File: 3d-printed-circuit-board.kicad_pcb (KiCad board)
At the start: 2 copper layers, 73.8 x 59.5 mm, 18 parts

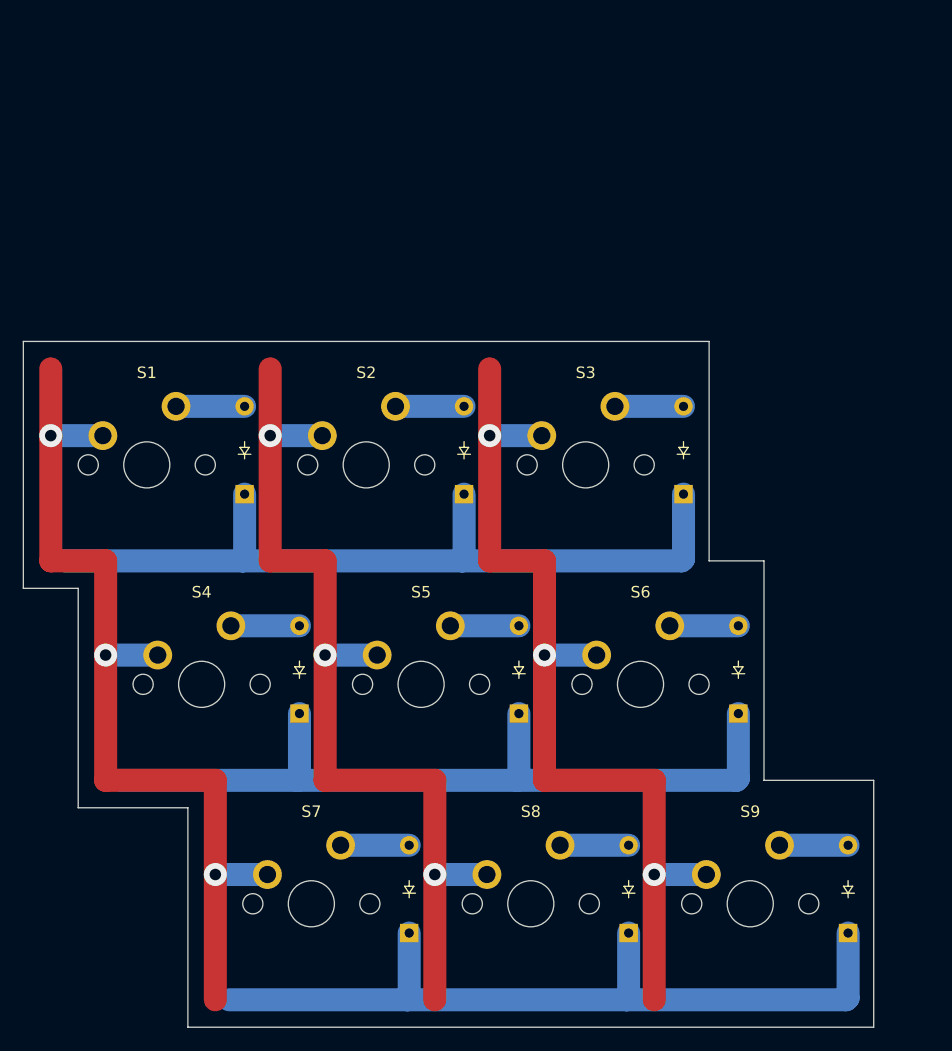
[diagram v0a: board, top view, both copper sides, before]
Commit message: Add MCU footprint
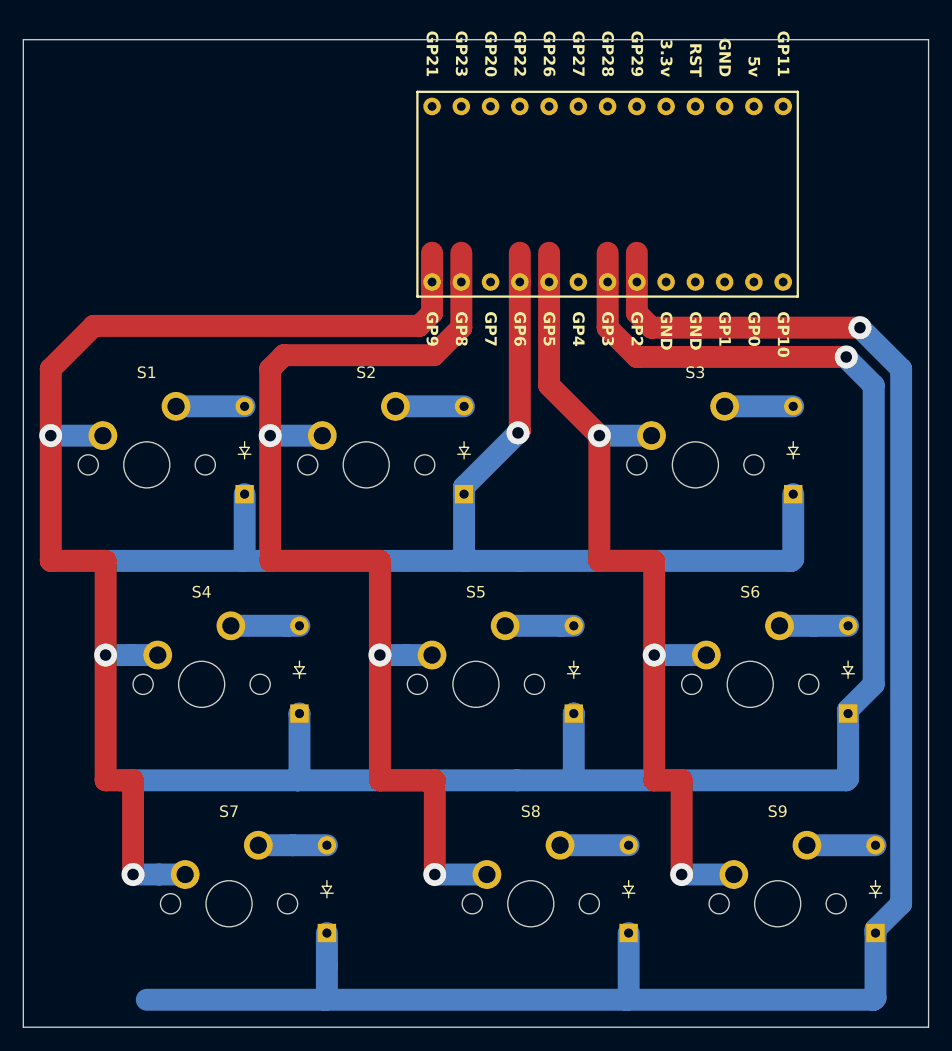
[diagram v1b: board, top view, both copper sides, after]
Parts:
- added U1: Arduino_Pro_Micro, ScottoKeebs_MCU:RP2040_Pro_Micro_Custom, B.Cu at (152.1, 66.9)
- moved S3 9.53 mm to (161.0, 90.4)
- moved S6 9.53 mm to (165.7, 109.4)
- moved D3 9.53 mm to (169.5, 92.9)
- moved D6 9.53 mm to (174.2, 112.0)
- moved D7 7.14 mm to (129.0, 131.0)
- moved S7 7.14 mm to (120.5, 128.5)
- moved S5 4.76 mm to (141.9, 109.4)
- moved D5 4.76 mm to (150.4, 112.0)
- moved S9 2.38 mm to (168.1, 128.5)
- moved D9 2.38 mm to (176.6, 131.0)
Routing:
- net ROW2: track 71.2 -> 163.4 mm, vias 0 -> 1
- net ROW1: track 71.2 -> 141.5 mm, vias 0 -> 1
- net ROW0: track 71.2 -> 103.6 mm, vias 0 -> 1
- net COL0: track 82.9 -> 109.5 mm
- net COL1: track 82.9 -> 98.7 mm
- net COL2: track 82.6 -> 76.3 mm
- net Net-(D6-A): track 5.95 -> 8.93 mm
- net Net-(D7-A): track 5.95 -> 8.93 mm
- net Net-(D5-A): track 5.95 -> 7.06 mm
- net Net-(D4-A): track 5.95 -> 7.06 mm
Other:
- board size 73.8 x 59.5 mm -> 78.6 x 85.7 mm

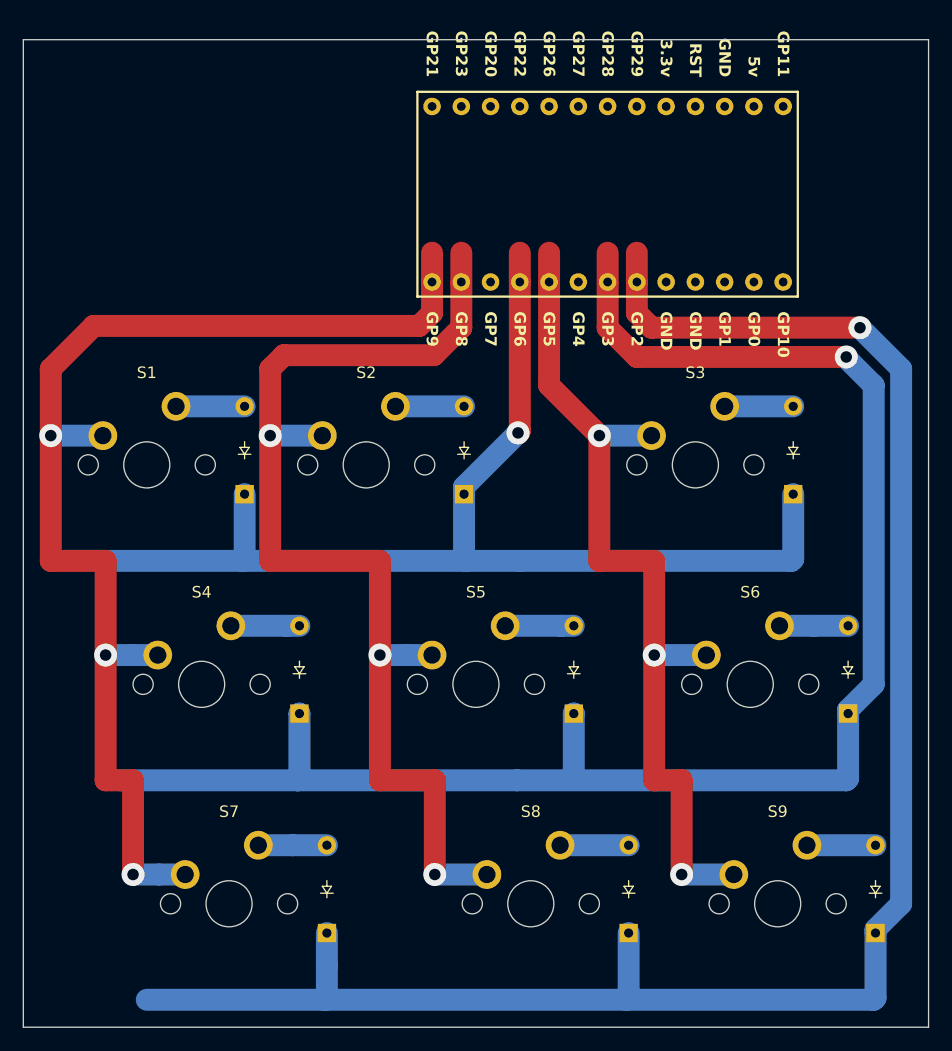
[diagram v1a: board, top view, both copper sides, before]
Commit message: Revise routing to reduce solder points
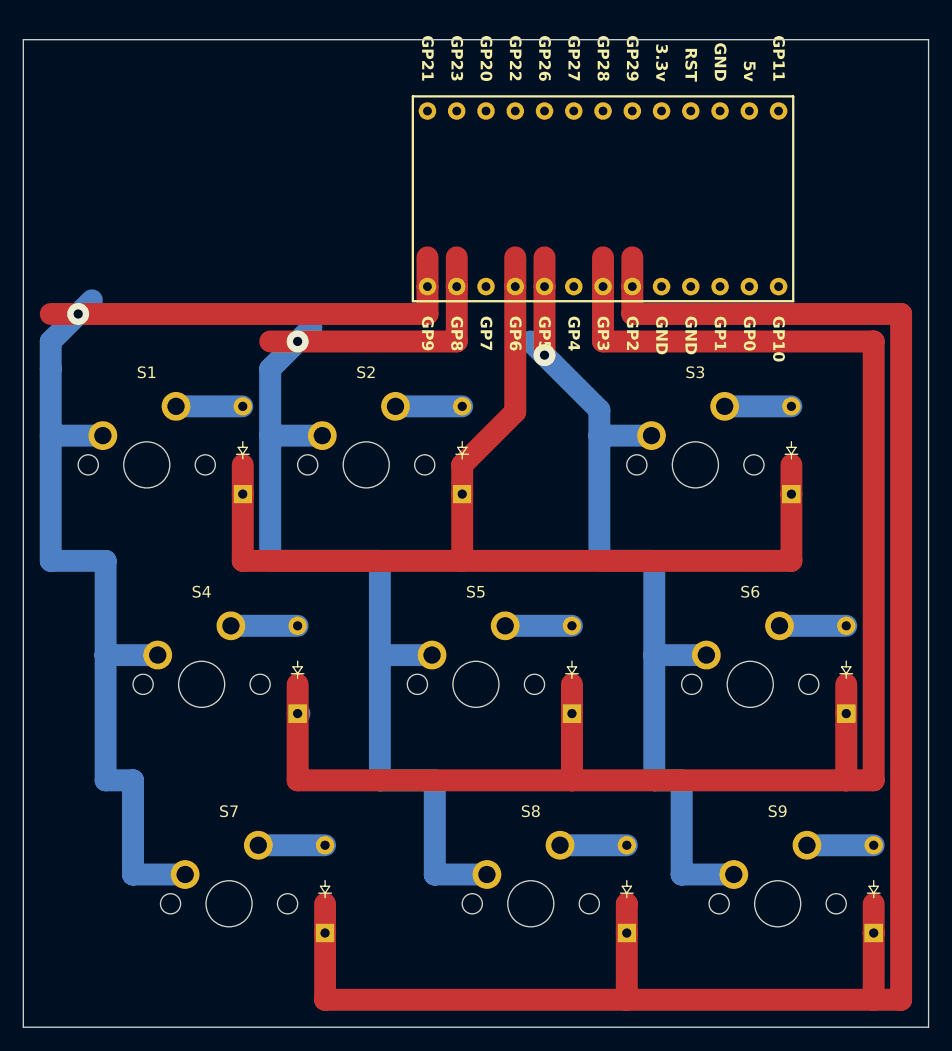
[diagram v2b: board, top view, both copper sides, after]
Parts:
- moved U1 0.56 mm to (151.7, 67.3)
- moved D1 0.16 mm to (121.7, 92.9)
- moved D2 0.16 mm to (140.7, 92.9)
- moved D3 0.16 mm to (169.3, 92.9)
- moved D4 0.16 mm to (126.4, 112.0)
- moved D5 0.16 mm to (150.3, 112.0)
- moved D6 0.16 mm to (174.1, 112.0)
- moved D7 0.16 mm to (128.8, 131.0)
- moved D8 0.16 mm to (155.0, 131.0)
- moved D9 0.16 mm to (176.4, 131.0)
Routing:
- net ROW0: track 103.6 -> 92.6 mm, vias 1 -> 0
- net Net-(D6-A): track 8.93 -> 5.79 mm
- net Net-(D7-A): track 8.93 -> 5.79 mm
- net ROW1: track 141.5 -> 143.9 mm, vias 1 -> 0
- net COL1: track 98.7 -> 100.3 mm, vias 3 -> 1
- net COL2: track 76.3 -> 78.0 mm, vias 3 -> 1
- net Net-(D5-A): track 7.06 -> 5.79 mm
- net Net-(D4-A): track 7.06 -> 5.79 mm
- net ROW2: track 163.4 -> 162.8 mm, vias 1 -> 0
- net COL0: track 109.5 -> 109.7 mm, vias 3 -> 1

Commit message: Route full hhkb layout
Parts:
- added D10: Diode, ScottoKeebs_Components:Diode_DO-35, B.Cu at (217.8, 40.6)
- added D11: Diode, ScottoKeebs_Components:Diode_DO-35, B.Cu at (236.9, 40.6)
- added D12: Diode, ScottoKeebs_Components:Diode_DO-35, B.Cu at (255.9, 40.6)
- added D13: Diode, ScottoKeebs_Components:Diode_DO-35, B.Cu at (275.0, 40.6)
- added D14: Diode, ScottoKeebs_Components:Diode_DO-35, B.Cu at (293.7, 24.1)
- added D16: Diode, ScottoKeebs_Components:Diode_DO-35, B.Cu at (51.1, 59.7)
- added D17: Diode, ScottoKeebs_Components:Diode_DO-35, B.Cu at (74.9, 59.7)
- added D18: Diode, ScottoKeebs_Components:Diode_DO-35, B.Cu at (94.0, 59.7)
- added D19: Diode, ScottoKeebs_Components:Diode_DO-35, B.Cu at (113.0, 59.7)
- added D20: Diode, ScottoKeebs_Components:Diode_DO-35, B.Cu at (132.1, 59.7)
- added D21: Diode, ScottoKeebs_Components:Diode_DO-35, B.Cu at (151.1, 59.7)
- added D22: Diode, ScottoKeebs_Components:Diode_DO-35, B.Cu at (170.2, 59.7)
- added D23: Diode, ScottoKeebs_Components:Diode_DO-35, B.Cu at (189.2, 59.7)
- added D24: Diode, ScottoKeebs_Components:Diode_DO-35, B.Cu at (208.3, 59.7)
- added D25: Diode, ScottoKeebs_Components:Diode_DO-35, B.Cu at (227.3, 59.7)
- added D26: Diode, ScottoKeebs_Components:Diode_DO-35, B.Cu at (246.4, 59.7)
- added D27: Diode, ScottoKeebs_Components:Diode_DO-35, B.Cu at (265.4, 59.7)
- added D28: Diode, ScottoKeebs_Components:Diode_DO-35, B.Cu at (284.5, 59.7)
- added D29: Diode, ScottoKeebs_Components:Diode_DO-35, B.Cu at (308.3, 59.7)
- added D30: Diode, ScottoKeebs_Components:Diode_DO-35, B.Cu at (53.5, 78.7)
- added D31: Diode, ScottoKeebs_Components:Diode_DO-35, B.Cu at (79.7, 78.7)
- added D32: Diode, ScottoKeebs_Components:Diode_DO-35, B.Cu at (98.7, 78.7)
- added D33: Diode, ScottoKeebs_Components:Diode_DO-35, B.Cu at (117.8, 78.7)
- added D34: Diode, ScottoKeebs_Components:Diode_DO-35, B.Cu at (136.8, 78.7)
- added D35: Diode, ScottoKeebs_Components:Diode_DO-35, B.Cu at (155.9, 78.7)
- added D36: Diode, ScottoKeebs_Components:Diode_DO-35, B.Cu at (174.9, 78.7)
- added D37: Diode, ScottoKeebs_Components:Diode_DO-35, B.Cu at (194.0, 78.7)
- added D38: Diode, ScottoKeebs_Components:Diode_DO-35, B.Cu at (213.0, 78.7)
- added D39: Diode, ScottoKeebs_Components:Diode_DO-35, B.Cu at (232.1, 78.7)
- added D40: Diode, ScottoKeebs_Components:Diode_DO-35, B.Cu at (251.1, 78.7)
- added D41: Diode, ScottoKeebs_Components:Diode_DO-35, B.Cu at (270.2, 78.7)
- added D42: Diode, ScottoKeebs_Components:Diode_DO-35, B.Cu at (287.6, 9.45)
- added D43: Diode, ScottoKeebs_Components:Diode_DO-35, B.Cu at (301.2, 78.7)
- added D44: Diode, ScottoKeebs_Components:Diode_DO-35, B.Cu at (58.3, 97.8)
- added D45: Diode, ScottoKeebs_Components:Diode_DO-35, B.Cu at (89.2, 97.8)
- added D46: Diode, ScottoKeebs_Components:Diode_DO-35, B.Cu at (108.3, 97.8)
- added D47: Diode, ScottoKeebs_Components:Diode_DO-35, B.Cu at (127.3, 97.8)
- added D48: Diode, ScottoKeebs_Components:Diode_DO-35, B.Cu at (146.4, 97.8)
- added D49: Diode, ScottoKeebs_Components:Diode_DO-35, B.Cu at (165.4, 97.8)
- added D50: Diode, ScottoKeebs_Components:Diode_DO-35, B.Cu at (184.5, 97.8)
- added D51: Diode, ScottoKeebs_Components:Diode_DO-35, B.Cu at (203.5, 97.8)
- added D52: Diode, ScottoKeebs_Components:Diode_DO-35, B.Cu at (222.6, 97.8)
- added D53: Diode, ScottoKeebs_Components:Diode_DO-35, B.Cu at (241.6, 97.8)
- added D54: Diode, ScottoKeebs_Components:Diode_DO-35, B.Cu at (260.7, 97.8)
- added D55: Diode, ScottoKeebs_Components:Diode_DO-35, B.Cu at (286.9, 97.8)
- added D56: Diode, ScottoKeebs_Components:Diode_DO-35, B.Cu at (313.1, 97.8)
- added D57: Diode, ScottoKeebs_Components:Diode_DO-35, B.Cu at (74.9, 116.8)
- added D58: Diode, ScottoKeebs_Components:Diode_DO-35, B.Cu at (98.7, 116.8)
- added D59: Diode, ScottoKeebs_Components:Diode_DO-35, B.Cu at (172.6, 116.8)
- added D60: Diode, ScottoKeebs_Components:Diode_DO-35, B.Cu at (246.4, 116.8)
- added D61: Diode, ScottoKeebs_Components:Diode_DO-35, B.Cu at (270.2, 116.8)
- added S10: Keyswitch, ScottoKeebs_MX:MX_PCB_1.00u, F.Cu at (209.6, 38.1)
- added S11: Keyswitch, ScottoKeebs_MX:MX_PCB_1.00u, F.Cu at (228.6, 38.1)
- added S12: Keyswitch, ScottoKeebs_MX:MX_PCB_1.00u, F.Cu at (247.7, 38.1)
- added S13: Keyswitch, ScottoKeebs_MX:MX_PCB_1.00u, F.Cu at (266.7, 38.1)
- added S14: Keyswitch, ScottoKeebs_MX:MX_PCB_1.00u, F.Cu at (285.8, 38.1)
- added S15: Keyswitch, ScottoKeebs_MX:MX_PCB_1.00u, F.Cu at (304.8, 38.1)
- added S16: Keyswitch, ScottoKeebs_MX:MX_PCB_1.00u, F.Cu at (42.9, 57.1)
- added S17: Keyswitch, ScottoKeebs_MX:MX_PCB_1.00u, F.Cu at (66.7, 57.1)
- added S18: Keyswitch, ScottoKeebs_MX:MX_PCB_1.00u, F.Cu at (85.7, 57.1)
- added S19: Keyswitch, ScottoKeebs_MX:MX_PCB_1.00u, F.Cu at (104.8, 57.1)
- added S20: Keyswitch, ScottoKeebs_MX:MX_PCB_1.00u, F.Cu at (123.8, 57.1)
- added S21: Keyswitch, ScottoKeebs_MX:MX_PCB_1.00u, F.Cu at (142.9, 57.1)
- added S22: Keyswitch, ScottoKeebs_MX:MX_PCB_1.00u, F.Cu at (161.9, 57.1)
- added S23: Keyswitch, ScottoKeebs_MX:MX_PCB_1.00u, F.Cu at (181.0, 57.1)
- added S24: Keyswitch, ScottoKeebs_MX:MX_PCB_1.00u, F.Cu at (200.0, 57.1)
- added S25: Keyswitch, ScottoKeebs_MX:MX_PCB_1.00u, F.Cu at (219.1, 57.1)
- added S26: Keyswitch, ScottoKeebs_MX:MX_PCB_1.00u, F.Cu at (238.1, 57.1)
- added S27: Keyswitch, ScottoKeebs_MX:MX_PCB_1.00u, F.Cu at (257.2, 57.1)
- added S28: Keyswitch, ScottoKeebs_MX:MX_PCB_1.00u, F.Cu at (276.2, 57.1)
- added S29: Keyswitch, ScottoKeebs_MX:MX_PCB_1.00u, F.Cu at (300.0, 57.1)
- added S30: Keyswitch, ScottoKeebs_MX:MX_PCB_1.00u, F.Cu at (45.2, 76.2)
- added S31: Keyswitch, ScottoKeebs_MX:MX_PCB_1.00u, F.Cu at (71.4, 76.2)
- added S32: Keyswitch, ScottoKeebs_MX:MX_PCB_1.00u, F.Cu at (90.5, 76.2)
- added S33: Keyswitch, ScottoKeebs_MX:MX_PCB_1.00u, F.Cu at (109.5, 76.2)
- added S34: Keyswitch, ScottoKeebs_MX:MX_PCB_1.00u, F.Cu at (128.6, 76.2)
- added S35: Keyswitch, ScottoKeebs_MX:MX_PCB_1.00u, F.Cu at (147.6, 76.2)
- added S36: Keyswitch, ScottoKeebs_MX:MX_PCB_1.00u, F.Cu at (166.7, 76.2)
- added S37: Keyswitch, ScottoKeebs_MX:MX_PCB_1.00u, F.Cu at (185.7, 76.2)
- added S38: Keyswitch, ScottoKeebs_MX:MX_PCB_1.00u, F.Cu at (204.8, 76.2)
- added S39: Keyswitch, ScottoKeebs_MX:MX_PCB_1.00u, F.Cu at (223.8, 76.2)
- added S40: Keyswitch, ScottoKeebs_MX:MX_PCB_1.00u, F.Cu at (242.9, 76.2)
- added S41: Keyswitch, ScottoKeebs_MX:MX_PCB_1.00u, F.Cu at (261.9, 76.2)
- added S42: Keyswitch, ScottoKeebs_MX:MX_PCB_1.00u, F.Cu at (292.9, 76.2)
- added S43: Keyswitch, ScottoKeebs_MX:MX_PCB_1.00u, F.Cu at (50.0, 95.2)
- added S44: Keyswitch, ScottoKeebs_MX:MX_PCB_1.00u, F.Cu at (81.0, 95.2)
- added S45: Keyswitch, ScottoKeebs_MX:MX_PCB_1.00u, F.Cu at (100.0, 95.2)
- added S46: Keyswitch, ScottoKeebs_MX:MX_PCB_1.00u, F.Cu at (119.1, 95.2)
- added S47: Keyswitch, ScottoKeebs_MX:MX_PCB_1.00u, F.Cu at (138.1, 95.2)
- added S48: Keyswitch, ScottoKeebs_MX:MX_PCB_1.00u, F.Cu at (157.2, 95.2)
- added S49: Keyswitch, ScottoKeebs_MX:MX_PCB_1.00u, F.Cu at (176.2, 95.2)
- added S50: Keyswitch, ScottoKeebs_MX:MX_PCB_1.00u, F.Cu at (195.3, 95.2)
- added S51: Keyswitch, ScottoKeebs_MX:MX_PCB_1.00u, F.Cu at (214.3, 95.2)
- added S52: Keyswitch, ScottoKeebs_MX:MX_PCB_1.00u, F.Cu at (233.4, 95.2)
- added S53: Keyswitch, ScottoKeebs_MX:MX_PCB_1.00u, F.Cu at (252.4, 95.2)
- added S54: Keyswitch, ScottoKeebs_MX:MX_PCB_1.00u, F.Cu at (278.6, 95.2)
- added S55: Keyswitch, ScottoKeebs_MX:MX_PCB_1.00u, F.Cu at (304.8, 95.2)
- added S56: Keyswitch, ScottoKeebs_MX:MX_PCB_1.00u, F.Cu at (66.7, 114.3)
- added S57: Keyswitch, ScottoKeebs_MX:MX_PCB_1.00u, F.Cu at (90.5, 114.3)
- added S58: Keyswitch, ScottoKeebs_MX:MX_PCB_1.00u, F.Cu at (164.3, 114.3)
- added S59: Keyswitch, ScottoKeebs_MX:MX_PCB_1.00u, F.Cu at (238.1, 114.3)
- added S60: Keyswitch, ScottoKeebs_MX:MX_PCB_1.00u, F.Cu at (261.9, 114.3)
- D1, D2, D3, D4, D5, D6, D7, D8, D9: moved to B.Cu
- U1: value Arduino_Pro_Micro -> Pro_Micro; footprint ScottoKeebs_MCU:RP2040_Pro_Micro_Custom -> ScottoKeebs_MCU:RP2040_Pro_Micro; moved to F.Cu
- moved D3 99.7 mm to (84.5, 40.6)
- moved S3 99.6 mm to (76.2, 38.1)
- moved S7 95.8 mm to (152.4, 38.1)
- moved D7 95.8 mm to (160.7, 40.6)
- moved S8 93.7 mm to (171.4, 38.1)
- moved D8 93.7 mm to (179.7, 40.6)
- moved S9 93.1 mm to (190.5, 38.1)
- moved D9 93.1 mm to (198.8, 40.6)
- moved D1 91.7 mm to (46.4, 40.6)
- moved D2 91.7 mm to (65.4, 40.6)
- moved S1 91.6 mm to (38.1, 38.1)
- moved S2 91.6 mm to (57.1, 38.1)
- moved D6 78.4 mm to (141.6, 40.6)
- moved S6 78.3 mm to (133.3, 38.1)
- moved D5 76.5 mm to (122.6, 40.6)
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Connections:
- D4 pad 1: ROW1 -> ROW0
- D5 pad 1: ROW1 -> ROW0
- D6 pad 1: ROW1 -> ROW0
- D7 pad 1: ROW2 -> ROW0
- D8 pad 1: ROW2 -> ROW0
- D9 pad 1: ROW2 -> ROW0
- S4 pad 1: COL0 -> COL3
- S5 pad 1: COL1 -> COL4
- S6 pad 1: COL2 -> COL5
- S7 pad 1: COL0 -> COL6
- S8 pad 1: COL1 -> COL7
- S9 pad 1: COL2 -> COL8
- U1 pad 1: (no net) -> COL4
- U1 pad 10: ROW0 -> COL9
- U1 pad 11: unconnected-(U1-GP7-Pad11) -> COL12
- U1 pad 12: COL1 -> COL11
- U1 pad 13: COL0 -> COL10
- U1 pad 19: unconnected-(U1-GP21-Pad19) -> ROW2
- U1 pad 2: unconnected-(U1-GP0-Pad2) -> COL3
- U1 pad 20: unconnected-(U1-GP23-Pad20) -> ROW1
- U1 pad 21: unconnected-(U1-GP20-Pad21) -> ROW0
- U1 pad 22: unconnected-(U1-GP22-Pad22) -> COL13
- U1 pad 24: unconnected-(U1-GP27-Pad24) -> COL1
- U1 pad 25: unconnected-(U1-GP28-Pad25) -> COL0
- U1 pad 26: unconnected-(U1-GP29-Pad26) -> ROW3
- U1 pad 3: unconnected-(U1-GP1-Pad3) -> COL2
- U1 pad 31: (no net) -> ROW4
- U1 pad 6: ROW2 -> COL5
- U1 pad 7: ROW1 -> COL6
- U1 pad 8: unconnected-(U1-GP4-Pad8) -> COL7
- U1 pad 9: COL2 -> COL8
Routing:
- net ROW3: track 0.00 -> 579.6 mm, vias 0 -> 1
- net ROW4: track 0.00 -> 483.3 mm, vias 0 -> 1
- net ROW0: track 92.6 -> 493.8 mm
- net ROW1: track 143.9 -> 542.5 mm, vias 0 -> 1
- net ROW2: track 162.8 -> 554.0 mm, vias 0 -> 1
- net COL13: track 0.00 -> 273.0 mm, vias 0 -> 4
- net COL12: track 0.00 -> 237.1 mm, vias 0 -> 4
- net COL11: track 0.00 -> 229.4 mm, vias 0 -> 5
- net COL3: track 0.00 -> 224.3 mm, vias 0 -> 5
- net COL10: track 0.00 -> 198.0 mm, vias 0 -> 5
- net COL2: track 78.0 -> 254.3 mm, vias 1 -> 5
- net COL6: track 0.00 -> 174.9 mm, vias 0 -> 5
- net COL4: track 0.00 -> 162.0 mm, vias 0 -> 4
- net COL1: track 100.3 -> 261.1 mm, vias 1 -> 4
- net COL5: track 0.00 -> 158.2 mm, vias 0 -> 4
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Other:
- board size 78.6 x 85.7 mm -> 290.5 x 116.7 mm
